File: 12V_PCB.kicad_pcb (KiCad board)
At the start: 2 copper layers, 15.5 x 31.5 mm, 8 parts, among them J1 12V IN, J2 RPI CONN, J3 BTN CONN, J4 LED CONN, Q1 PMV40UN2R

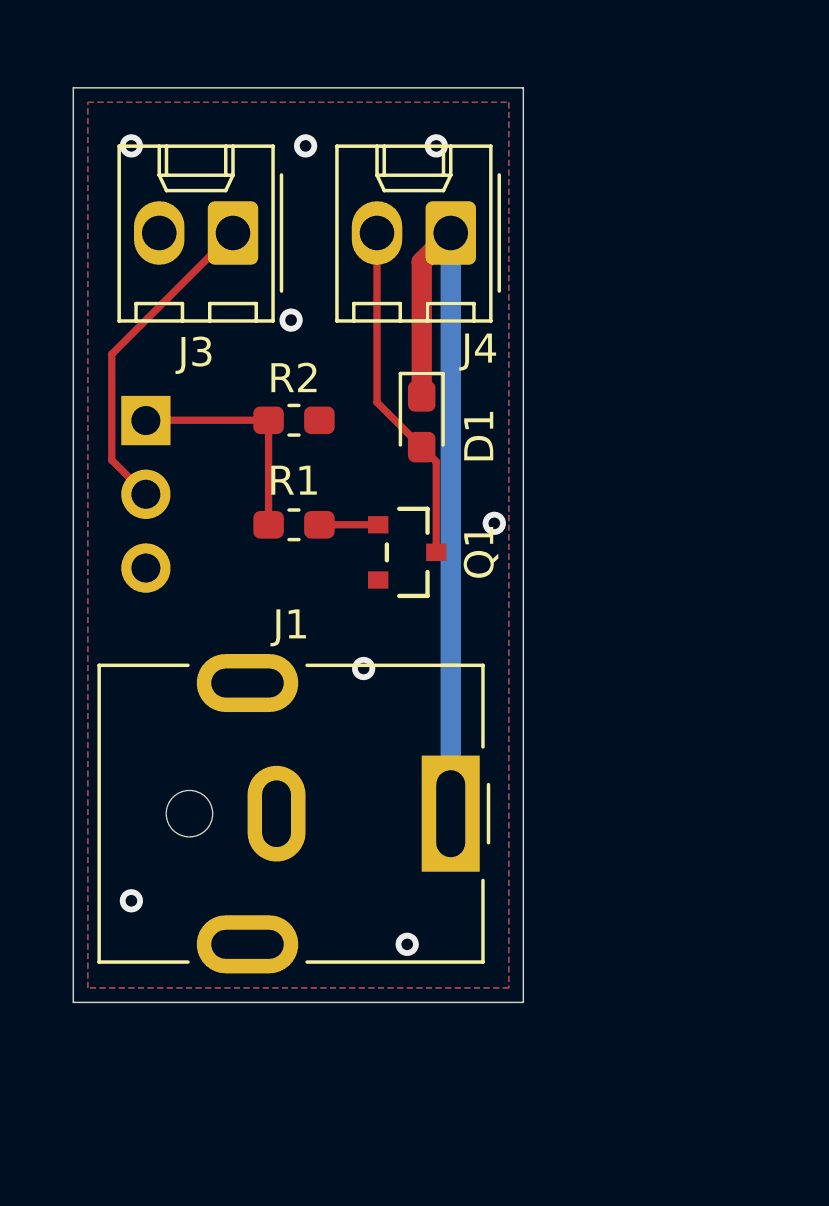
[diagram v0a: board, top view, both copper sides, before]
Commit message: added LED_BTN section
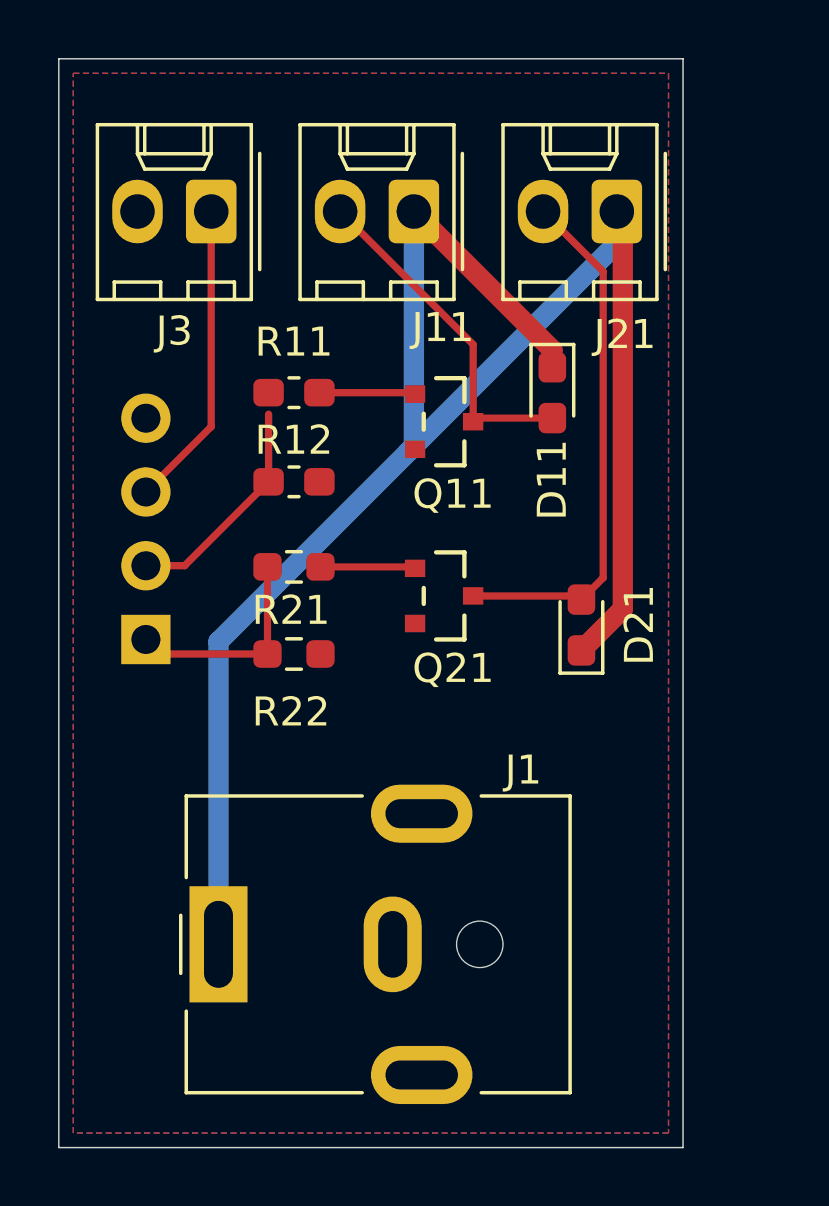
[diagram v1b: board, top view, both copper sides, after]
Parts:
- removed D1: SL04-E3-08, Diode_SMD:D_0603_1608Metric_Pad1.05x0.95mm_HandSolder
- added D11: SL04-E3-08, Diode_SMD:D_0603_1608Metric_Pad1.05x0.95mm_HandSolder, F.Cu at (170.5, 118.0)
- added D21: SL04-E3-08, Diode_SMD:D_0603_1608Metric_Pad1.05x0.95mm_HandSolder, F.Cu at (171.5, 126.0)
- added J21: LED_BTN, Connector_Molex:Molex_KK-254_AE-6410-02A_1x02_P2.54mm_Vertical, F.Cu at (172.7, 111.8)
- added Q21: PMV40UN2R, PMV40UN2R:Nexperia-SOT23-01_2018-0-0, F.Cu at (166.8, 125.0)
- added R21: 1k, Resistor_SMD:R_0603_1608Metric_Pad0.98x0.95mm_HandSolder, F.Cu at (161.6, 124.0)
- added R22: 10k, Resistor_SMD:R_0603_1608Metric_Pad0.98x0.95mm_HandSolder, F.Cu at (161.6, 127.0)
- J11: renamed from J4; value LED CONN -> LED_STRIP
- J2: footprint Connector_PinSocket_2.54mm:PinSocket_1x03_P2.54mm_Vertical -> Connector_PinSocket_2.54mm:PinSocket_1x04_P2.54mm_Vertical
- J3: value BTN CONN -> BTN
- moved J1 9.18 mm to (159.0, 137.0), turned to 90 degrees
- moved J2 7.54 mm to (156.5, 126.5), turned to 0 degrees
- moved Q11 4.68 mm to (166.8, 119.0)
- moved R11 4.55 mm to (161.6, 118.0)
- moved R12 2.12 mm to (161.6, 121.1)
- moved J11 1.47 mm to (165.7, 111.8)
- moved J3 1.05 mm to (158.8, 111.8)
- renumbered Q1 to Q11, R1 to R11, R2 to R12
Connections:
- J2 pad 1: LED -> LED_BTN
- J2 pad 2: BTN -> LED_STRIP
- J2 pad 3: GND -> BTN
- R11 pad 2: LED -> LED_STRIP
- R12 pad 1: LED -> LED_STRIP
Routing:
- net +12V: track 26.0 -> 63.0 mm
- net Net-(D21-Pad2): track 0.00 -> 18.3 mm
- net LED: track 7.83 -> 0.00 mm
- net LED_STRIP: track 0.00 -> 7.75 mm
- net LED_BTN: track 0.00 -> 7.39 mm
- net Net-(Q21-Pad1): track 0.00 -> 3.28 mm
- net Net-(Q11-Pad1): track 2.03 -> 3.32 mm
- net BTN: track 11.2 -> 10.6 mm
- net GND: vias 8 -> 0
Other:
- board size 15.5 x 31.5 mm -> 21.5 x 37.5 mm

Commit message: Final version with panelization
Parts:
- removed D11, D21: SL04-E3-08, Diode_SMD:D_0603_1608Metric_Pad1.05x0.95mm_HandSolder
- J1: footprint Connector_BarrelJack:BarrelJack_CUI_PJ-063AH_Horizontal -> Connector_BarrelJack:BarrelJack_Horizontal
- Q11, Q21: value PMV40UN2R -> IRLL2705PBF; footprint PMV40UN2R:Nexperia-SOT23-01_2018-0-0 -> Package_TO_SOT_SMD:SOT-223-3_TabPin2
- moved Q21 3.38 mm to (169.5, 127.0), turned to 0 degrees
- moved Q11 2.78 mm to (169.5, 119.5), turned to 0 degrees
- moved J21 2.29 mm to (175.0, 112.0)
- moved J11 1.29 mm to (167.0, 112.0)
- moved J1 1.00 mm to (159.0, 136.0), turned to 180 degrees
- moved J3 0.24 mm to (158.8, 112.0)
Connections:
- J11 pad 1: +12V -> Net-(J11-Pad1)
- J11 pad 2: Net-(D11-Pad2) -> +12V
- J21 pad 1: +12V -> Net-(J21-Pad1)
- J21 pad 2: Net-(D21-Pad2) -> +12V
- Q11 pad 2: GND -> Net-(J11-Pad1)
- Q11 pad 3: Net-(D11-Pad2) -> GND
- Q21 pad 2: GND -> Net-(J21-Pad1)
- Q21 pad 3: Net-(D21-Pad2) -> GND
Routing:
- net Net-(D21-Pad2): track 18.3 -> 0.00 mm
- net Net-(J21-Pad1): track 0.00 -> 18.2 mm
- net +12V: track 63.0 -> 46.0 mm
- net Net-(D11-Pad2): track 11.9 -> 0.00 mm
- net Net-(J11-Pad1): track 0.00 -> 10.1 mm
- net Net-(Q11-Pad1): track 3.32 -> 4.21 mm
- net Net-(Q21-Pad1): track 3.28 -> 4.13 mm
- net LED_STRIP: track 7.75 -> 8.49 mm
- net GND: vias 0 -> 16
- added copper zone on F.Cu, net Net-(J11-Pad1)
- added copper zone on F.Cu, net Net-(J21-Pad1)
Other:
- board size 21.5 x 37.5 mm -> 24.5 x 32.5 mm
- net class +12V: clearance 0.2 -> 0.5; trace_width 0.7 -> 2
- net class 12V signal added: clearance 0.2, trace_width 1, via_dia 0.8, via_drill 0.4
- board text added: "+12V"
- board text added: "12V IN"
- board text added: "BTN"
- board text added: "BTN LED"
- board text added: "GND"
- board text added: "LED_BTN"
- board text added: "STRIP"
